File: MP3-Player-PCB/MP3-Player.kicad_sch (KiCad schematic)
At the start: 0 parts

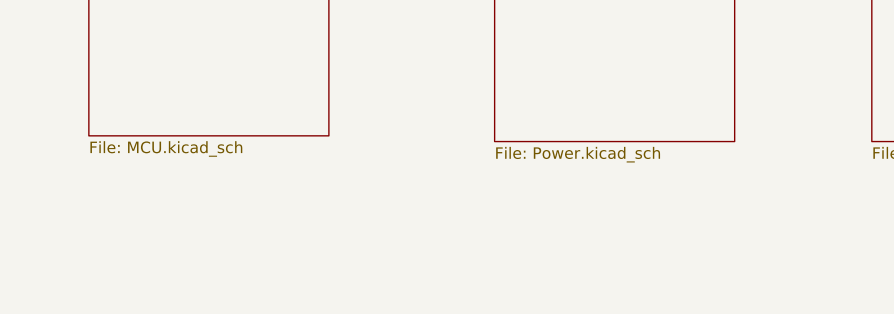
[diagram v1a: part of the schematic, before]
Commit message: Added button circuitry
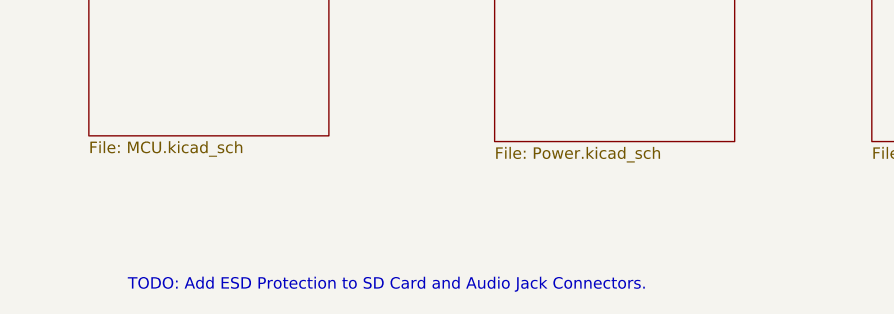
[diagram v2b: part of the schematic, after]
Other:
- note added: "TODO: Add ESD Protection to SD Card and Audio Jack Connectors."
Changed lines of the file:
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@@
+		)
+	)
+	(text "TODO: Add ESD Protection to SD Card and Audio Jack Connectors."
+		(exclude_from_sim no)
+		(at 73.152 106.172 0)
+		(effects
+			(font
+				(size 1.27 1.27)
+			)
 		)
 	)

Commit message: Added adc pin and voltage divider to read battery voltage. Also added charging status leds, and assigned some footprints
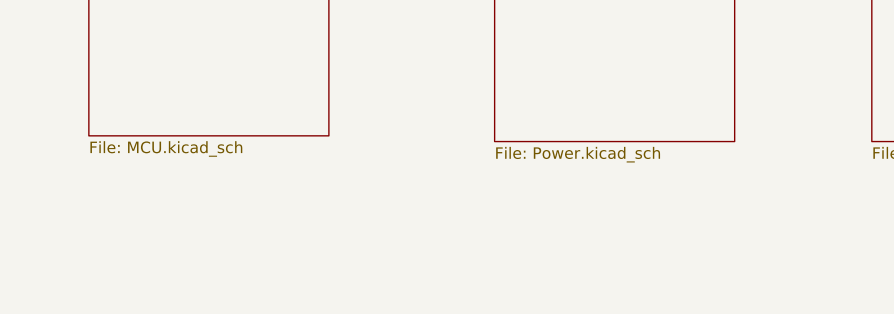
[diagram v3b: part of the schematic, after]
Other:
- note removed: "TODO: Add ESD Protection to SD Card and Audio Jack Connectors."
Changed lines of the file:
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@@
-		)
-	)
-	(text "TODO: Add ESD Protection to SD Card and Audio Jack Connectors."
-		(exclude_from_sim no)
-		(at 73.152 106.172 0)
-		(effects
-			(font
-				(size 1.27 1.27)
-			)
 		)
 	)
